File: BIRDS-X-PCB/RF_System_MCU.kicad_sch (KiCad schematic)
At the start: 20 parts, among them J1 Conn_01x03, SW401 SW_Push, U2 24LC32A/SN, U402 STM32L432KCU6

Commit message: Clean up heirarchy
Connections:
- net UART_BOSS_TO_TNC_OPT: no longer names the net of U402.30 (PB7)
- net UART_TNC_TO_BOSS_OPT: no longer names the net of U402.29 (PB6)
- no-connect marks 7 -> 9
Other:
- note removed: "UART1 - Optional Mission Boss Commands Normally Disabled"
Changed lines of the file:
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@@
   )
   (no_connect (at 158.75 93.98))
+  (no_connect (at 158.75 86.36))
+  (no_connect (at 158.75 83.82))
   (no_connect (at 127 71.12))
   (no_connect (at 127 76.2))
@@
     (stroke (width 0) (type default))
   )
-  (wire (pts (xy 158.75 86.36) (xy 162.56 86.36))
-    (stroke (width 0) (type default))
-  )
   (wire (pts (xy 171.45 29.21) (xy 171.45 33.02))
     (stroke (width 0) (type default))
@@
     (stroke (width 0) (type default))
   )
-  (wire (pts (xy 158.75 83.82) (xy 162.56 83.82))
-    (stroke (width 0) (type default))
-  )
   (wire (pts (xy 123.19 73.66) (xy 127 73.66))
     (stroke (width 0) (type default))
@@
   (wire (pts (xy 179.07 99.06) (xy 179.07 101.6))
     (stroke (width 0) (type default))
-  )
-  (text "UART1 - Optional Mission Boss Commands\nNormally Disabled"
-    (at 187.96 87.63 0)
-    (effects (font (size 1.27 1.27)) (justify left bottom))
   )
   (text "Bypass for MCU" (at 172.72 31.75 0)
@@
     )
   )
-  (hierarchical_label "UART_BOSS_TO_TNC_OPT" (shape input) (at 162.56 86.36 0) (fields_autoplaced)
-    (effects (font (size 1.27 1.27)) (justify left))
-  )
   (hierarchical_label "UART_TNC_TO_JASPER" (shape output) (at 123.19 73.66 180) (fields_autoplaced)
     (effects (font (size 1.27 1.27)) (justify right))
@@
     (effects (font (size 1.27 1.27)) (justify right))
   )
-  (hierarchical_label "UART_TNC_TO_BOSS_OPT" (shape output) (at 162.56 83.82 0) (fields_autoplaced)
-    (effects (font (size 1.27 1.27)) (justify left))
-  )
   (hierarchical_label "TNC_DAC_AUDIO" (shape output) (at 123.19 78.74 180) (fields_autoplaced)

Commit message: Schematic updates
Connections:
- net +3V3: now also C402.1, U402.5 (VDDA/VREF+)
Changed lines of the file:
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@@
   (junction (at 171.45 33.02) (diameter 0) (color 0 0 0 0)
+  )
+  (junction (at 189.23 67.31) (diameter 0) (color 0 0 0 0)
   )
   (junction (at 168.91 99.06) (diameter 0) (color 0 0 0 0)
@@
   )
   (wire (pts (xy 113.03 86.36) (xy 127 86.36))
+    (stroke (width 0) (type default))
+  )
+  (wire (pts (xy 189.23 63.5) (xy 189.23 67.31))
     (stroke (width 0) (type default))
   )
@@
         )
       )
+    )
+  )
+  (symbol (lib_id "power:+3V3") (at 189.23 63.5 0) (unit 1)
+    (in_bom yes) (on_board yes) (dnp no) (fields_autoplaced)
+    (property "Reference" "#PWR0408" (at 189.23 67.31 0)
+      (effects (font (size 1.27 1.27)) hide)
+    )
+    (property "Value" "+3V3" (at 189.23 59.69 0)
+      (effects (font (size 1.27 1.27)))
+    )
+    (property "Footprint" "" (at 189.23 63.5 0)
+      (effects (font (size 1.27 1.27)) hide)
+    )
+    (property "Datasheet" "" (at 189.23 63.5 0)
+      (effects (font (size 1.27 1.27)) hide)
+    )
+    (pin "1")
+    (instances
+      (project "BIRDS-X-PCB"
+        (path "/c2796b15-795a-4d6e-ad4b-0ba87ded4bc9/d490f402-3a4d-40a5-b165-30c74c6560b7"
+          (reference "#PWR0408") (unit 1)
+        )
+        (path "/c2796b15-795a-4d6e-ad4b-0ba87ded4bc9/245c031a-1c72-4f7a-bf07-271990525459/99e8c1ae-7e35-4da7-a263-12b7b7656438"
+          (reference "#PWR01011") (unit 1)
+        )
+      )

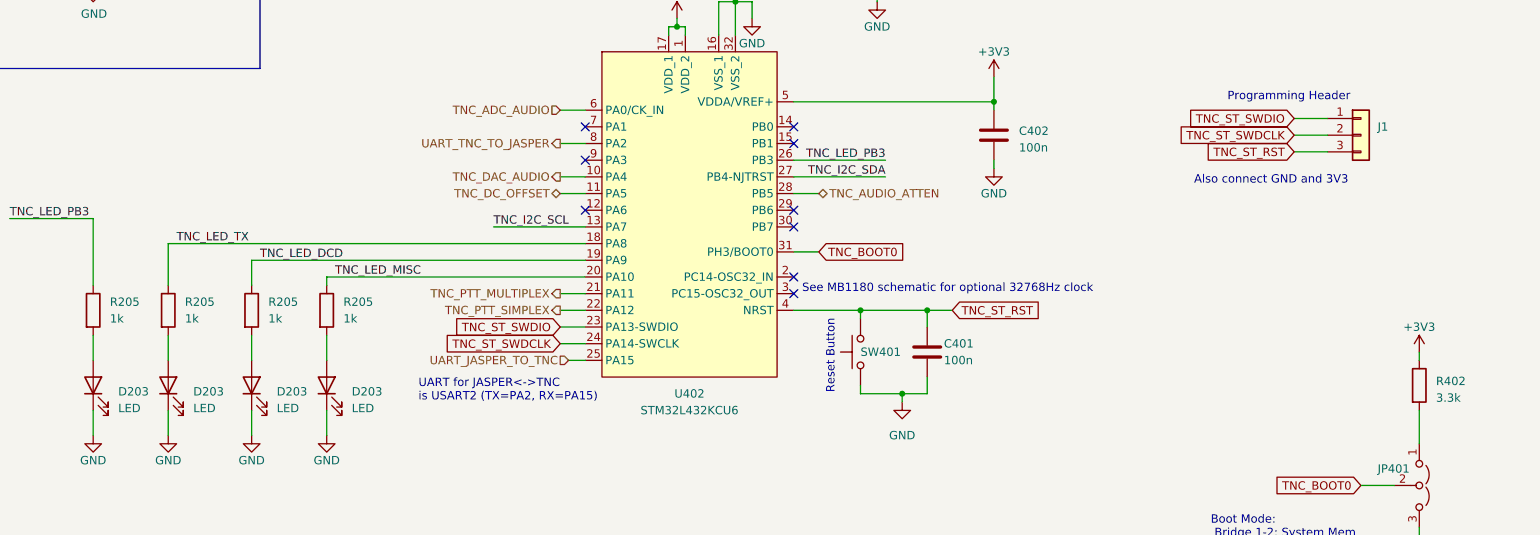
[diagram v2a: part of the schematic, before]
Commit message: Assign remaining footprints, fix Annotations
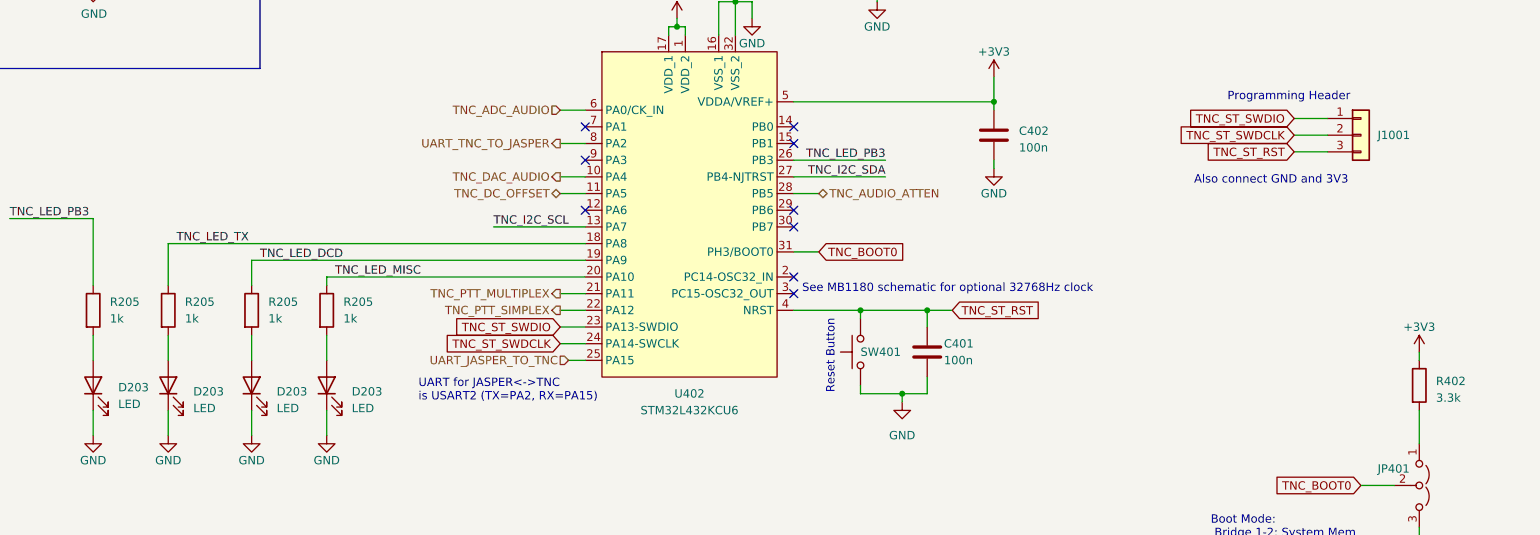
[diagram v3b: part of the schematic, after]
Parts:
- J1001: renamed from J1; footprint (none) -> Connector_PinHeader_1.27mm:PinHeader_1x03_P1.27mm_Vertical
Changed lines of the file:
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@@
   (symbol (lib_id "Connector_Generic:Conn_01x03") (at 245.11 72.39 0) (unit 1)
     (in_bom yes) (on_board yes) (dnp no) (fields_autoplaced)
-    (property "Reference" "J1" (at 247.65 71.12 0)
+    (property "Reference" "J1001" (at 247.65 72.39 0)
       (effects (font (size 1.27 1.27)) (justify left))
     )
@@
       (effects (font (size 1.27 1.27)) (justify left) hide)
     )
-    (property "Footprint" "" (at 245.11 72.39 0)
+    (property "Footprint" "Connector_PinHeader_1.27mm:PinHeader_1x03_P1.27mm_Vertical" (at 245.11 72.39 0)
       (effects (font (size 1.27 1.27)) hide)
     )
@@
       (project "BIRDS-X-PCB"
         (path "/c2796b15-795a-4d6e-ad4b-0ba87ded4bc9/245c031a-1c72-4f7a-bf07-271990525459/99e8c1ae-7e35-4da7-a263-12b7b7656438"
-          (reference "J1") (unit 1)
+          (reference "J1001") (unit 1)
         )
       )
@@
         )
         (path "/c2796b15-795a-4d6e-ad4b-0ba87ded4bc9/245c031a-1c72-4f7a-bf07-271990525459/99e8c1ae-7e35-4da7-a263-12b7b7656438"
-          (reference "R1") (unit 1)
+          (reference "R1006") (unit 1)
         )
       )
@@
         )
         (path "/c2796b15-795a-4d6e-ad4b-0ba87ded4bc9/245c031a-1c72-4f7a-bf07-271990525459/99e8c1ae-7e35-4da7-a263-12b7b7656438"
-          (reference "C1") (unit 1)
+          (reference "C1005") (unit 1)
         )
       )
@@
         )
         (path "/c2796b15-795a-4d6e-ad4b-0ba87ded4bc9/245c031a-1c72-4f7a-bf07-271990525459/99e8c1ae-7e35-4da7-a263-12b7b7656438"
-          (reference "C2") (unit 1)
+          (reference "C1004") (unit 1)
         )
       )
@@
         )
         (path "/c2796b15-795a-4d6e-ad4b-0ba87ded4bc9/245c031a-1c72-4f7a-bf07-271990525459/99e8c1ae-7e35-4da7-a263-12b7b7656438"
-          (reference "U1") (unit 1)
+          (reference "U1002") (unit 1)
         )
       )
@@
   (symbol (lib_id "Device:LED") (at 52.07 110.49 90) (unit 1)
     (in_bom yes) (on_board yes) (dnp no) (fields_autoplaced)
-    (property "Reference" "D203" (at 55.88 111.4425 90)
+    (property "Reference" "D203" (at 55.88 110.8075 90)
       (effects (font (size 1.27 1.27)) (justify right))
     )
-    (property "Value" "LED" (at 55.88 113.9825 90)
+    (property "Value" "LED" (at 55.88 113.3475 90)
       (effects (font (size 1.27 1.27)) (justify right))
     )
@@
         )
         (path "/c2796b15-795a-4d6e-ad4b-0ba87ded4bc9/245c031a-1c72-4f7a-bf07-271990525459/99e8c1ae-7e35-4da7-a263-12b7b7656438"
-          (reference "D1") (unit 1)
-        )
-      )
+          (reference "D1004") (unit 1)
+        )
+      )

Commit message: Major layout
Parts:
- U402: footprint Package_DFN_QFN:UFQFPN-32-1EP_5x5mm_P0.5mm_EP3.5x3.5mm_ThermalVias -> Package_DFN_QFN:UFQFPN-32-1EP_5x5mm_P0.5mm_EP3.5x3.5mm
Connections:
- net GND: now also U402.33 (GND_EP)
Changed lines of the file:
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@@
+    (stroke (width 0) (type default))
+  )
+  (wire (pts (xy 160.02 104.14) (xy 158.75 104.14))
     (stroke (width 0) (type default))
   )
@@
   )
   (wire (pts (xy 76.2 95.25) (xy 76.2 91.44))
+    (stroke (width 0) (type default))
+  )
+  (wire (pts (xy 160.02 104.14) (xy 160.02 114.3))
     (stroke (width 0) (type default))
   )
@@
       (effects (font (size 1.27 1.27)))
     )
-    (property "Footprint" "Package_DFN_QFN:UFQFPN-32-1EP_5x5mm_P0.5mm_EP3.5x3.5mm_ThermalVias" (at 139.7 114.3 0)
+    (property "Footprint" "Package_DFN_QFN:UFQFPN-32-1EP_5x5mm_P0.5mm_EP3.5x3.5mm" (at 139.7 114.3 0)
       (effects (font (size 1.27 1.27)) hide)
     )
@@
     (pin "31")
     (pin "32")
+    (pin "33")
     (pin "4")
     (pin "5")
@@
         )
       )
+    )
+  )
+  (symbol (lib_id "power:GND") (at 160.02 114.3 0) (unit 1)
+    (in_bom yes) (on_board yes) (dnp no) (fields_autoplaced)
+    (property "Reference" "#PWR0403" (at 160.02 120.65 0)
+      (effects (font (size 1.27 1.27)) hide)
+    )
+    (property "Value" "GND" (at 160.02 119.38 0)
+      (effects (font (size 1.27 1.27)))
+    )
+    (property "Footprint" "" (at 160.02 114.3 0)
+      (effects (font (size 1.27 1.27)) hide)
+    )
+    (property "Datasheet" "" (at 160.02 114.3 0)
+      (effects (font (size 1.27 1.27)) hide)
+    )
+    (pin "1")
+    (instances
+      (project "BIRDS-X-PCB"
+        (path "/c2796b15-795a-4d6e-ad4b-0ba87ded4bc9/d490f402-3a4d-40a5-b165-30c74c6560b7"
+          (reference "#PWR0403") (unit 1)
+        )
+        (path "/c2796b15-795a-4d6e-ad4b-0ba87ded4bc9/245c031a-1c72-4f7a-bf07-271990525459/99e8c1ae-7e35-4da7-a263-12b7b7656438"
+          (reference "#PWR01012") (unit 1)
+        )
+      )

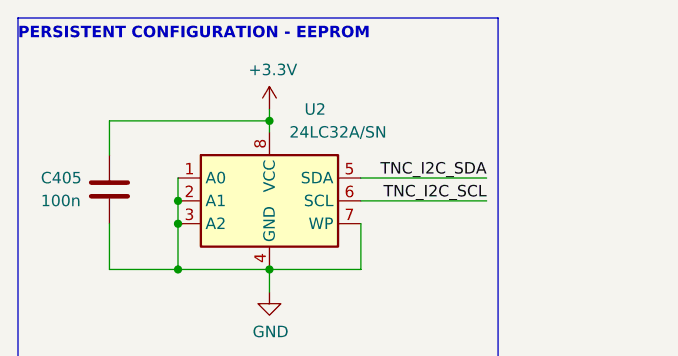
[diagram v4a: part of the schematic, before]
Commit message: Do most of routing
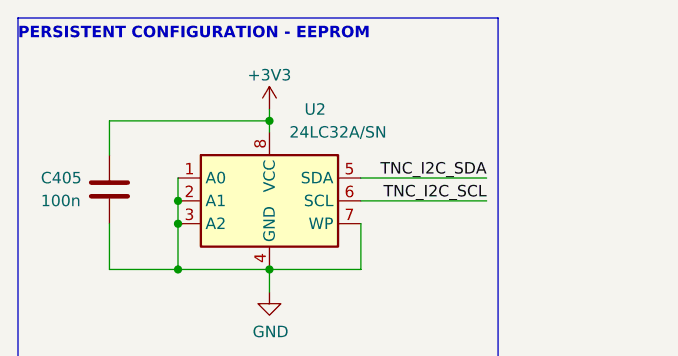
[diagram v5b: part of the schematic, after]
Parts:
- D203: footprint LED_SMD:LED_1206_3216Metric_Pad1.42x1.75mm_HandSolder -> LED_SMD:LED_0603_1608Metric
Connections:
- net +3.3V is gone; now on net +3V3: C405.1, U2.8 (VCC)
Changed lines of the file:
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@@
       (effects (font (size 1.27 1.27)) (justify right))
     )
-    (property "Footprint" "LED_SMD:LED_1206_3216Metric_Pad1.42x1.75mm_HandSolder" (at 63.5 110.49 0)
+    (property "Footprint" "LED_SMD:LED_0603_1608Metric" (at 63.5 110.49 0)
       (effects (font (size 1.27 1.27)) hide)
     )
@@
         (path "/c2796b15-795a-4d6e-ad4b-0ba87ded4bc9/245c031a-1c72-4f7a-bf07-271990525459/99e8c1ae-7e35-4da7-a263-12b7b7656438"
           (reference "R1006") (unit 1)
+        )
+      )
+    )
+  )
+  (symbol (lib_id "power:+3V3") (at 52.07 29.21 0) (unit 1)
+    (in_bom yes) (on_board yes) (dnp no) (fields_autoplaced)
+    (property "Reference" "#PWR0405" (at 52.07 33.02 0)
+      (effects (font (size 1.27 1.27)) hide)
+    )
+    (property "Value" "+3V3" (at 52.07 25.4 0)
+      (effects (font (size 1.27 1.27)))
+    )
+    (property "Footprint" "" (at 52.07 29.21 0)
+      (effects (font (size 1.27 1.27)) hide)
+    )
+    (property "Datasheet" "" (at 52.07 29.21 0)
+      (effects (font (size 1.27 1.27)) hide)
+    )
+    (pin "1")
+    (instances
+      (project "BIRDS-X-PCB"
+        (path "/c2796b15-795a-4d6e-ad4b-0ba87ded4bc9/d490f402-3a4d-40a5-b165-30c74c6560b7"
+          (reference "#PWR0405") (unit 1)
+        )
+        (path "/c2796b15-795a-4d6e-ad4b-0ba87ded4bc9/245c031a-1c72-4f7a-bf07-271990525459/99e8c1ae-7e35-4da7-a263-12b7b7656438"
+          (reference "#PWR010") (unit 1)
         )
       )
@@
       (effects (font (size 1.27 1.27)) (justify right))
     )
-    (property "Footprint" "LED_SMD:LED_1206_3216Metric_Pad1.42x1.75mm_HandSolder" (at 87.63 110.49 0)
+    (property "Footprint" "LED_SMD:LED_0603_1608Metric" (at 87.63 110.49 0)
       (effects (font (size 1.27 1.27)) hide)
     )
@@
       (effects (font (size 1.27 1.27)) (justify right))
     )
-    (property "Footprint" "LED_SMD:LED_1206_3216Metric_Pad1.42x1.75mm_HandSolder" (at 76.2 110.49 0)
+    (property "Footprint" "LED_SMD:LED_0603_1608Metric" (at 76.2 110.49 0)
       (effects (font (size 1.27 1.27)) hide)
     )
@@
         (path "/c2796b15-795a-4d6e-ad4b-0ba87ded4bc9/245c031a-1c72-4f7a-bf07-271990525459/99e8c1ae-7e35-4da7-a263-12b7b7656438"
           (reference "#PWR01010") (unit 1)
-        )
-      )
-    )
-  )
-  (symbol (lib_id "power:+3.3V") (at 52.07 29.21 0) (unit 1)
-    (in_bom yes) (on_board yes) (dnp no)
-    (property "Reference" "#PWR013" (at 52.07 33.02 0)
-      (effects (font (size 1.27 1.27)) hide)
-    )
-    (property "Value" "+3.3V" (at 52.451 24.8158 0)
-      (effects (font (size 1.27 1.27)))
-    )
-    (property "Footprint" "" (at 52.07 29.21 0)
-      (effects (font (size 1.27 1.27)) hide)
-    )
-    (property "Datasheet" "" (at 52.07 29.21 0)
-      (effects (font (size 1.27 1.27)) hide)
-    )
-    (pin "1")
-    (instances
-      (project "Nucleo32TNC"
-        (path "/37506541-f8e9-4000-b77e-5435dd7f86b3"
-          (reference "#PWR013") (unit 1)
-        )
-      )
-      (project "BIRDS-X-PCB"
-        (path "/c2796b15-795a-4d6e-ad4b-0ba87ded4bc9/245c031a-1c72-4f7a-bf07-271990525459"
-          (reference "#PWR0501") (unit 1)
-        )
-        (path "/c2796b15-795a-4d6e-ad4b-0ba87ded4bc9/245c031a-1c72-4f7a-bf07-271990525459/99e8c1ae-7e35-4da7-a263-12b7b7656438"
-          (reference "#PWR010") (unit 1)
         )
       )
@@
       (effects (font (size 1.27 1.27)) (justify right))
     )
-    (property "Footprint" "LED_SMD:LED_1206_3216Metric_Pad1.42x1.75mm_HandSolder" (at 52.07 110.49 0)
-      (effects (font (size 1.27 1.27)) hide)
-    )
+    (property "Footprint" "LED_SMD:LED_0603_1608Metric" (at 52.07 110.49 0)
+      (effects (font (size 1.27 1.27)) hide)
+    )
